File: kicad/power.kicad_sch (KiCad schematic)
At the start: 0 parts

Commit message: +/-15V power supply
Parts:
- added C84, C85, C86, C87, C88, C89: 10uF, symbol Device:C
- added D11, D12: D_Schottky, symbol Device:D_Schottky
- added R62, R97, R98: 10k, symbol Device:R_US
- added R94: 499k, symbol Device:R_US
- added R95: 100k, symbol Device:R_US
- added R96: 118k, symbol Device:R_US
- added R99: 127k, symbol Device:R_US
- added T1: 475uH, WE-PPTI_1006:WE-PPTI_1006_L10.2W6.73H4.19, symbol openmic:WE-PPTI_1006
- added U22: SN6505BDBV, Package_TO_SOT_SMD:SOT-23-6, symbol Power_Management:SN6505BDBV
- added U23: TPS7A39, Package_SON:Texas_S-PVSON-N10_ThermalVias, symbol Regulator_Linear:TPS7A39
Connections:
- new net: R62.1, U22.5 (EN)
- new net: R96.2, R97.1, U23.9 (FBP)
- new net: C88.1, U23.3 (NR/SS)
- new net: T1.3, U22.1 (D1)
- new net: T1.1, U22.3 (D2)
- new net: C86.2, D12.2 (A), U23.5 (INN)
- new net: C85.1, D11.1 (K), R94.1, U23.1 (INP)
- new net: D11.2 (A), D12.1 (K), T1.6
- new net: C87.1, R94.2, R95.1, U23.2 (EN)
- new net: R98.1, U23.8 (BUF)
- new net +15V: C89.1, R96.1, U23.10 (OUTP)
- new net +5V_USB: C84.1, R62.2, T1.2, U22.2 (VCC)
- new net -15V: R98.2, R99.1, R99.2, U23.6 (OUTN), U23.7 (FBN)
- new net GNDA: C84.2, C85.2, C86.1, C87.2, C88.2, C89.2, R95.2, R97.2, T1.4, U22.4 (GND), U23.11 (GND), U23.4 (GND)

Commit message: power supplies
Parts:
- added C106, C107: 1uF, symbol Device:C
- added C91, C94: 22uF, symbol Device:C
- added C92, C93: 10uF, symbol Device:C
- added L2, L3: 2.2uH, symbol Device:L
- added R100, R101: 100k, symbol Device:R_US
- added U24: TPS62172DSG, Package_SON:WSON-8-1EP_2x2mm_P0.5mm_EP0.9x1.6mm_ThermalVias, symbol Regulator_Switching:TPS62172DSG
- added U25: TPS62171DSG, Package_SON:WSON-8-1EP_2x2mm_P0.5mm_EP0.9x1.6mm_ThermalVias, symbol Regulator_Switching:TPS62171DSG
- added U26: TPS7A2009, Package_SON:Texas_X2SON-4_1x1mm_P0.65mm, symbol Regulator_Linear:TPS7A20xxxDQN
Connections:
- net +5V_USB: now also C92.1, C93.1, U24.2 (VIN), U24.3 (EN), U25.2 (VIN), U25.3 (EN)
- net GNDA: now also C106.2, C107.2, C91.2, C92.2, C93.2, C94.2, U24.1 (PGND), U24.4 (AGND), U24.5 (FB), U24.9 (PAD), U25.1 (PGND), U25.4 (AGND), U25.5 (FB), U25.9 (PAD), U26.2 (GND), U26.5 (Pad)
- new net: L3.1, U25.7 (SW)
- new net: R101.2, U25.8 (PG)
- new net: R100.2, U24.8 (PG)
- new net: L2.1, U24.7 (SW)
- new net +0V9: C107.1, U26.1 (OUT)
- new net +1V8: C106.1, C94.1, L3.2, R101.1, U25.6 (VOS), U26.3 (EN), U26.4 (IN)
- new net +3V3: C91.1, L2.2, R100.1, U24.6 (VOS)

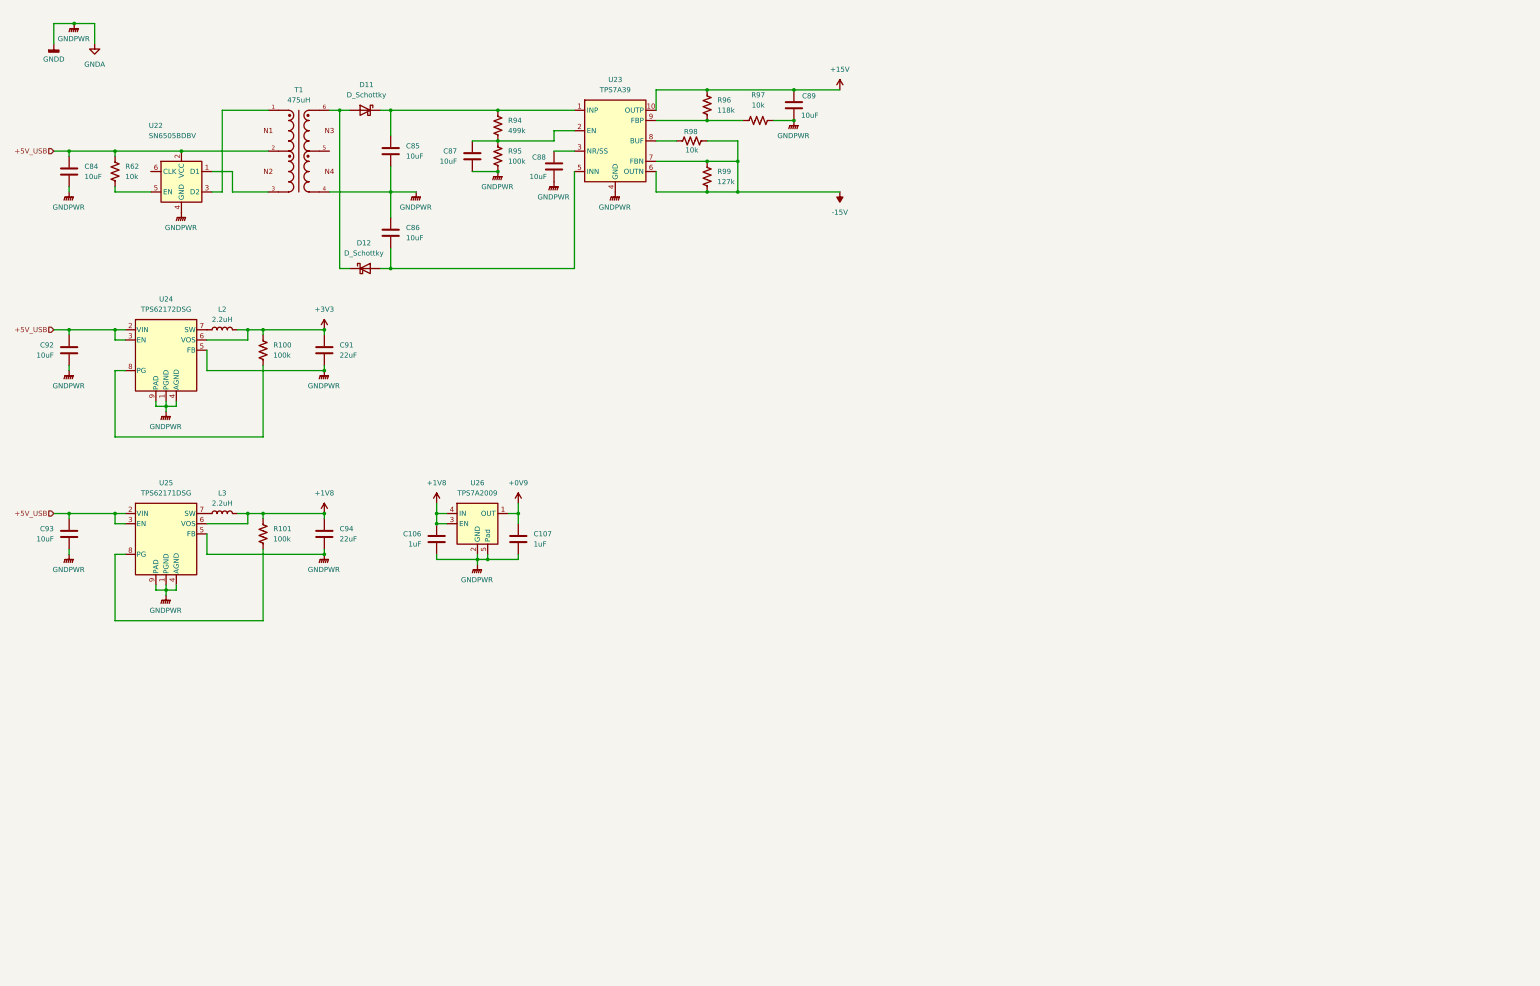
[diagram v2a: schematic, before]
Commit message: moved phantom power to power supply
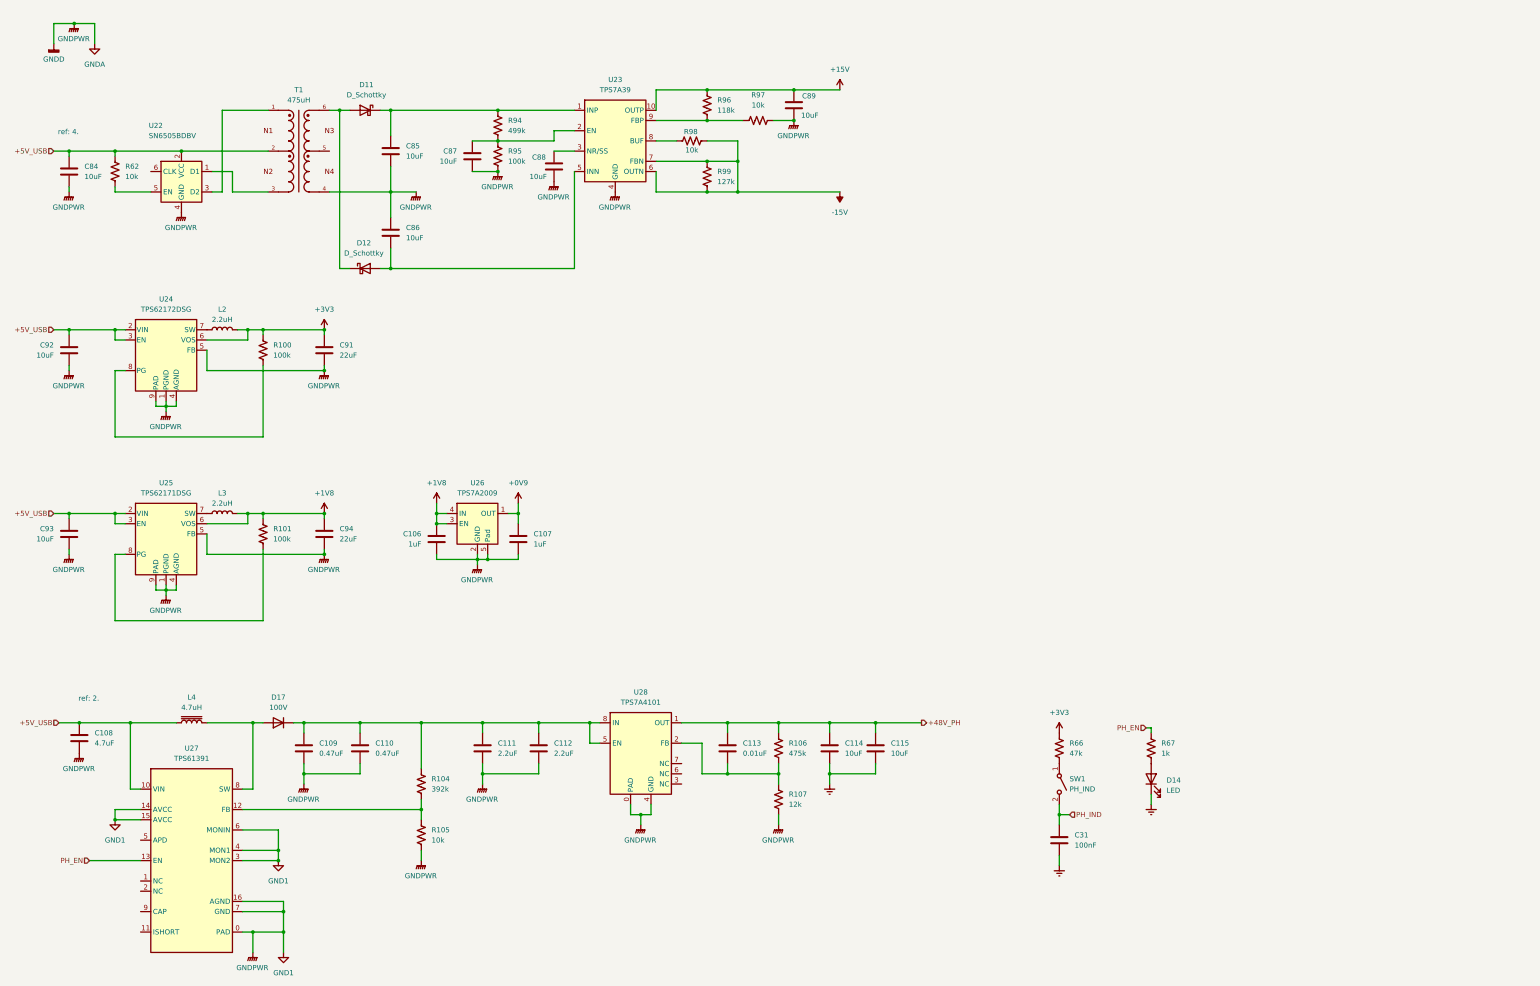
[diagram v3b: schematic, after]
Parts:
- added C108: 4.7uF, symbol Device:C
- added C109, C110: 0.47uF, symbol Device:C
- added C111, C112: 2.2uF, symbol Device:C
- added C113: 0.01uF, symbol Device:C
- added C114, C115: 10uF, symbol Device:C
- added C31: 100nF, symbol Device:C
- added D14: LED, symbol Device:LED
- added D17: 100V, symbol Device:D
- added L4: 4.7uH, symbol Device:L_Iron
- added R104: 392k, symbol Device:R_US
- added R105: 10k, symbol Device:R_US
- added R106: 475k, symbol Device:R_US
- added R107: 12k, symbol Device:R_US
- added R66: 47k, symbol Device:R_US
- added R67: 1k, symbol Device:R_US
- added SW1: PH_IND, symbol Switch:SW_SPST
- added U27: TPS61391, symbol openmic:TPS61391
- added U28: TPS7A4101, symbol openmic:TPS7A4101
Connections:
- net +3V3: now also R66.1
- net +5V_USB: now also C108.1, L4.1, U27.10 (VIN)
- net GNDA renamed GND1
- net GND1: now also C108.2, C109.2, C110.2, C111.2, C112.2, R105.2, R107.2, U27.0 (PAD), U27.14 (AVCC), U27.15 (AVCC), U27.16 (AGND), U27.3 (MON2), U27.4 (MON1), U27.6 (MONIN), U27.7 (GND), U28.0 (PAD), U28.4 (GND)
- new net: C109.1, C110.1, C111.1, C112.1, D17.1 (K), R104.1, U28.5 (EN), U28.8 (IN)
- new net: R66.2, SW1.1 (A)
- new net: D17.2 (A), L4.2, U27.8 (SW)
- new net: C113.2, R106.2, R107.1, U28.2 (FB)
- new net: R104.2, R105.1, U27.12 (FB)
- new net: D14.2 (A), R67.2
- new net +48V_PH: C113.1, C114.1, C115.1, R106.1, U28.1 (OUT)
- new net Earth: C114.2, C115.2, C31.2, D14.1 (K)
- new net PH_EN: R67.1, U27.13 (EN)
- new net PH_IND: C31.1, SW1.2 (B)
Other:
- note added: "ref: 2."
- note added: "ref: 4."

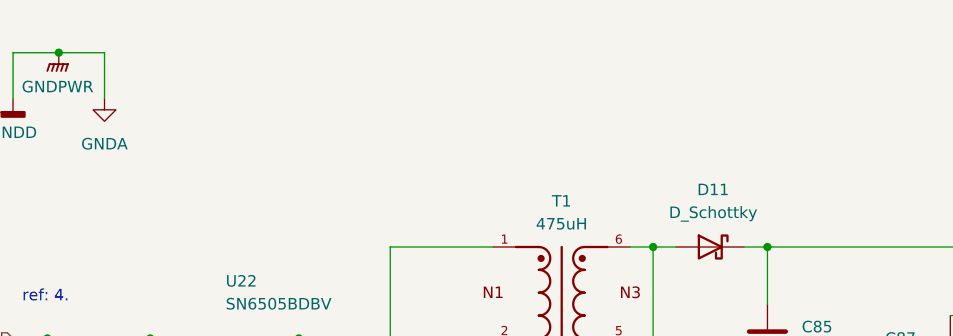
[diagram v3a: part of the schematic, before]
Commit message: WS2812 input array
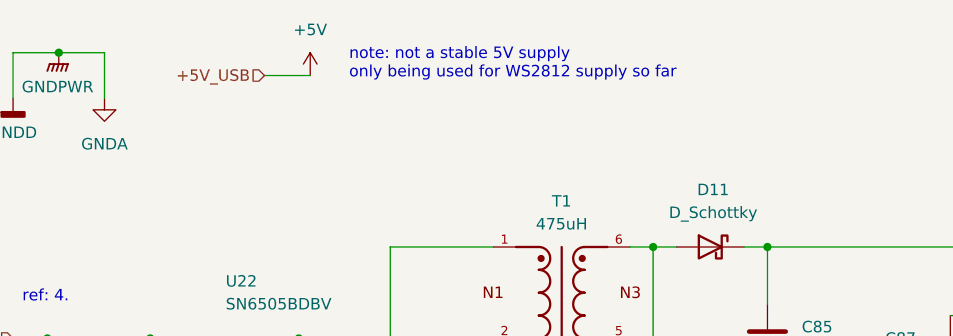
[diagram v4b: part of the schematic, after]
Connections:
- net +5V_USB renamed +5V
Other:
- note added: "note: not a stable 5V supply only being used for WS2812 supply so far"
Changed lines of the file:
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@@
 	(generator_version "9.0")
 	(paper "B")
+	(text "note: not a stable 5V supply\nonly being used for WS2812 supply so far"
+		(exclude_from_sim no)
+		(at 64.008 24.13 0)
+		(effects
+			(font
+				(size 1.27 1.27)
+			)
+			(justify left)
+		)
+	)
 	(text "ref: 4."
 		(exclude_from_sim no)
@@
 	(wire
 		(pts
+			(xy 54.61 25.4) (xy 59.69 25.4)
+		)
+		(stroke
+			(width 0)
+			(type default)
+		)
+	)
+	(wire
+		(pts
 			(xy 196.85 52.07) (xy 189.23 52.07)
 		)
@@
 		)
 	)
+	(hierarchical_label "+5V_USB"
+		(shape input)
+		(at 54.61 25.4 180)
+		(effects
+			(font
+				(size 1.27 1.27)
+			)
+			(justify right)
+		)
+	)
 	(symbol
 		(lib_id "Device:C")
@@
 					(unit 1)
 				)
+			)
+		)
+	)
+	(symbol
+		(lib_id "power:+5V")
+		(at 59.69 25.4 0)
+		(unit 1)
+		(exclude_from_sim no)
+		(in_bom yes)
+		(on_board yes)
+		(dnp no)
+		(fields_autoplaced yes)
+		(property "Reference" "#PWR066"
+			(at 59.69 29.21 0)
+			(effects
+				(font
+					(size 1.27 1.27)
+				)
+				(hide yes)
+			)
+		)
+		(property "Value" "+5V"
+			(at 59.69 20.32 0)
+			(effects
+				(font
+					(size 1.27 1.27)
+				)
+			)
+		)
+		(property "Footprint" ""
+			(at 59.69 25.4 0)
+			(effects
+				(font
+					(size 1.27 1.27)
+				)
+				(hide yes)
+			)
+		)
+		(property "Datasheet" ""
+			(at 59.69 25.4 0)
+			(effects
+				(font
+					(size 1.27 1.27)
+				)
+				(hide yes)
+			)
+		)
+		(property "Description" "Power symbol creates a global label with name \"+5V\""
+			(at 59.69 25.4 0)
+			(effects
+				(font
+					(size 1.27 1.27)
+				)
+				(hide yes)
+			)
+		)
+		(pin "1"
+		)
+		(instances
+			(project "openmic"
+				(path "/84faeadc-8b12-4a66-a17f-5c56e5923fb8/4ba50981-e4e9-4615-8d45-25e1b83d5dc4"
+					(reference "#PWR066")
+					(unit 1)
+				)

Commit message: #11
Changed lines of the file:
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@@
 	)
 	(hierarchical_label "PH_IND"
-		(shape input)
+		(shape output)
 		(at 279.4 219.71 0)
 		(effects

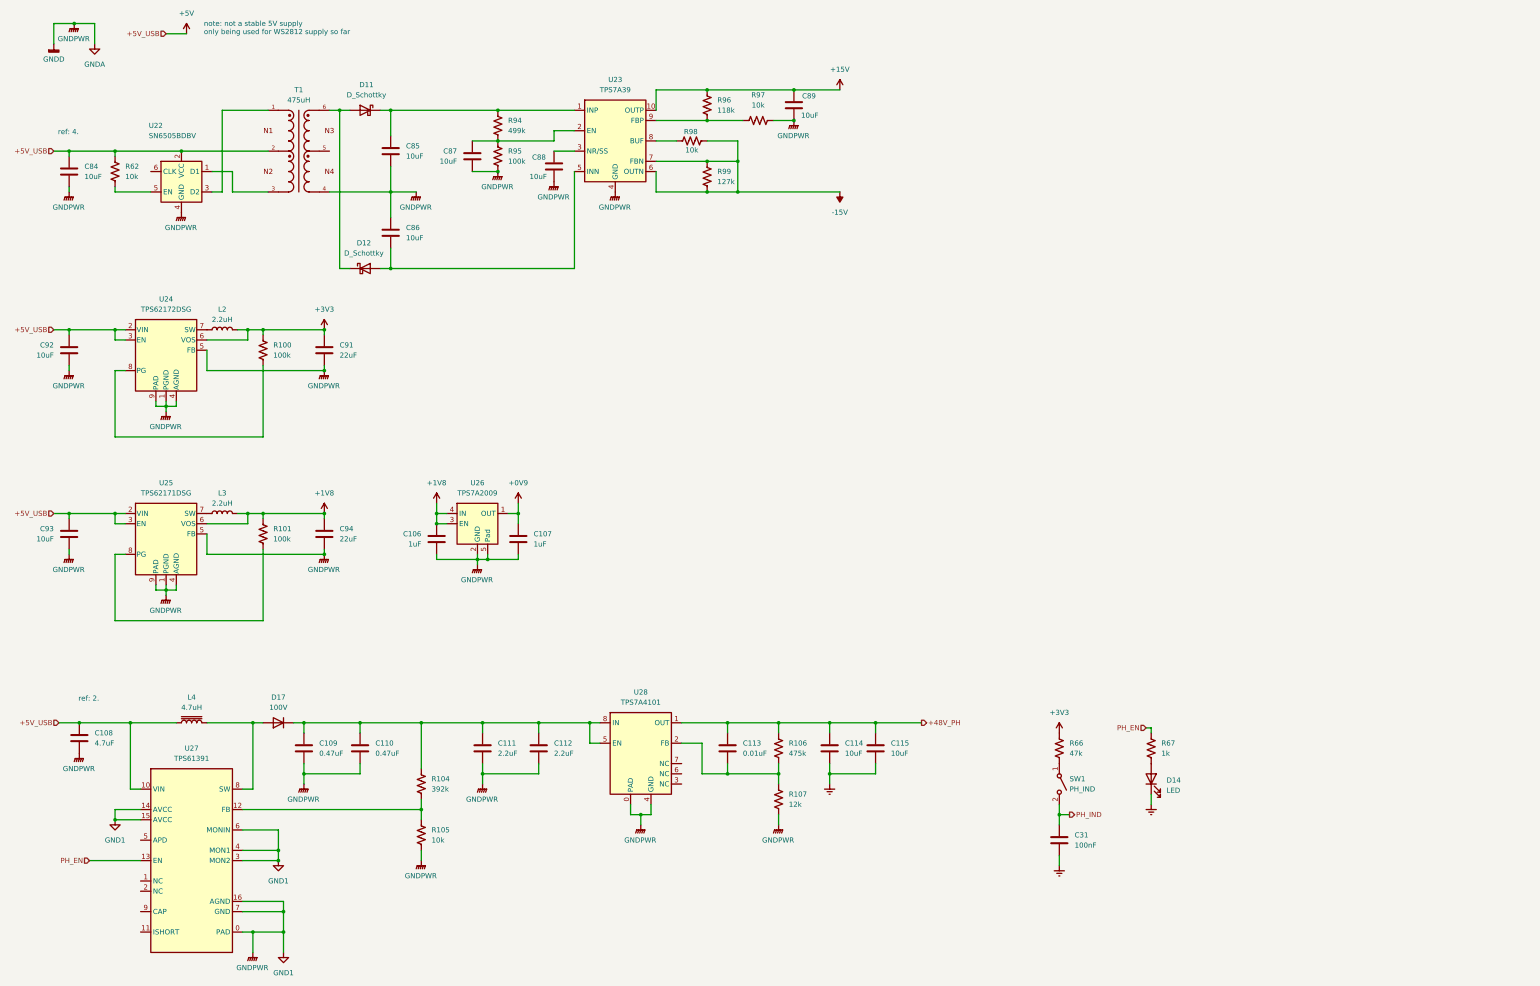
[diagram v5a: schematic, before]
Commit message: external power supply (#9)
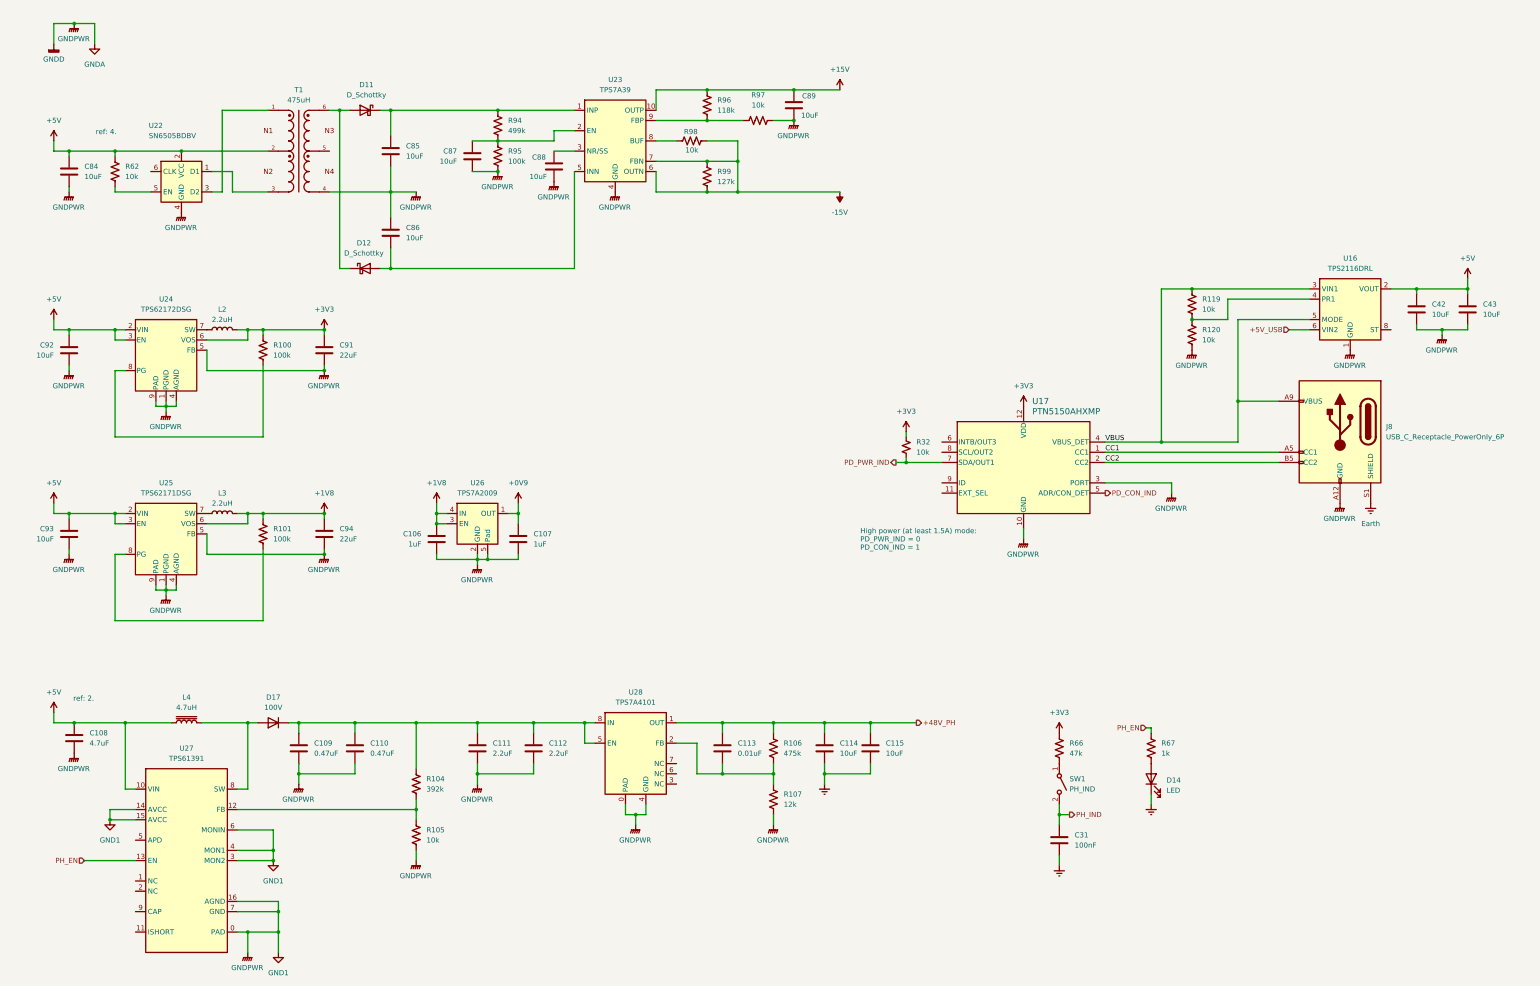
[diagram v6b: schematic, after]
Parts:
- added C42, C43: 10uF, symbol Device:C
- added J8: USB_C_Receptacle_PowerOnly_6P, symbol Connector:USB_C_Receptacle_PowerOnly_6P
- added R119, R120: 10k, symbol Device:R_US
- added R32: 10k, symbol Device:R_Small_US
- added U16: TPS2116DRL, Package_TO_SOT_SMD:SOT-583-8, symbol Power_Management:TPS2116DRL
- added U17: PTN5150AHXMP, SOT1355-1_X2QFN12_NXP, symbol openmic:PTN5150AHXMP
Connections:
- net +3V3: now also R32.1, U17.12 (VDD)
- net +5V: now also C42.1, C43.1, U16.2 (VOUT), U16.7 (VOUT)
- net Earth: now also J8.S1 (SHIELD)
- net GND1: now also C42.2, C43.2, J8.A12 (GND), J8.B12 (GND), R120.2, U16.1 (GND), U17.10 (GND), U17.3 (PORT)
- new net: R119.2, R120.1, U16.4 (PR1)
- new net +5V_USB: U16.6 (VIN2)
- new net CC1: J8.A5 (CC1), U17.1 (CC1)
- new net CC2: J8.B5 (CC2), U17.2 (CC2)
- new net PD_CON_IND: U17.5 (ADR/CON_DET)
- new net PD_PWR_IND: R32.2, U17.7 (SDA/OUT1)
- new net VBUS: J8.A9 (VBUS), J8.B9 (VBUS), R119.1, U16.3 (VIN1), U16.5 (MODE), U17.4 (VBUS_DET)
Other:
- note added: "High power (at least 1.5A) mode: PD_PWR_IND = 0 PD_CON_IND = 1"
- note removed: "note: not a stable 5V supply only being used for WS2812 supply so far"
- moved on the sheet: C108, C109, C110, C111, C112, C113, C114, C115, D17, L4, R104, R105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
